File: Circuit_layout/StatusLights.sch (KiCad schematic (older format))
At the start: 33 parts, among them Q1 ZVP4525G, U1 PDM2-S24-S12, U11 TLP293, U12 TLP293, U16 LTC3638

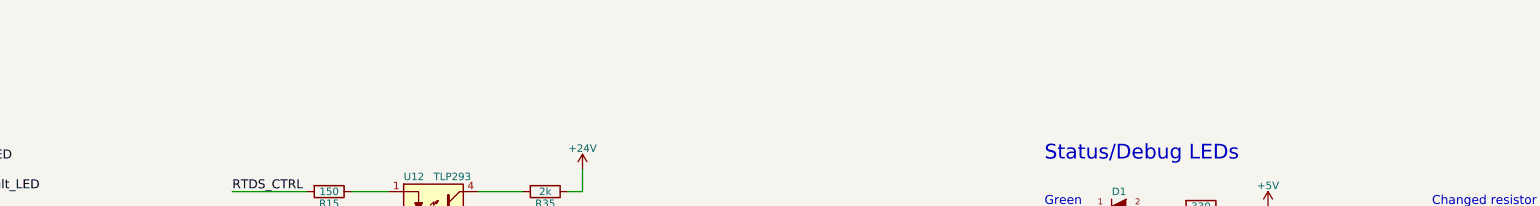
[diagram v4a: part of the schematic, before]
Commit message: reviewed schematic w/ prof. nadovich. proposed changes
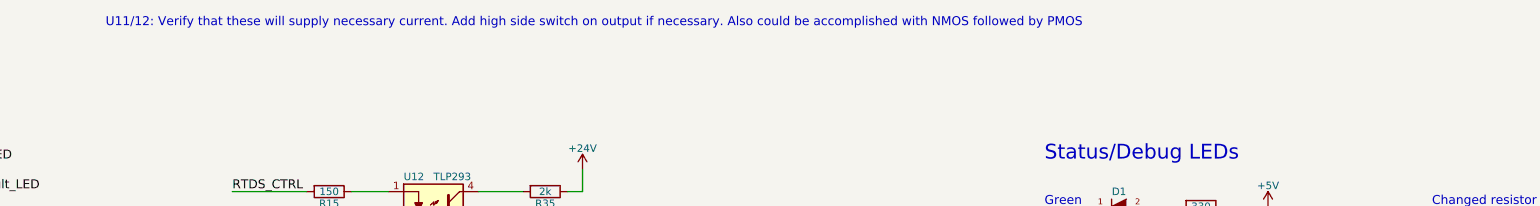
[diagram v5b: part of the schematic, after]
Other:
- note added: "U11/12: Verify that these will supply necessary current. Add high side switch on output if necessary. Also could be accomplished with NMOS followed by PMOS"
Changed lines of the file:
@@
 	6800 5200 6800 5300
 Connection ~ 6800 5300
+Text Notes 2450 -100 0    60   ~ 0
+U11/12: Verify that these will supply necessary current. Add high side switch on output if necessary. Also could be accomplished with NMOS followed by PMOS
 $EndSCHEMATC

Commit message: small changes
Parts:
- removed R84: 1k, Resistors_SMD:R_0805_HandSoldering, symbol R
- added R17: 10k, Resistors_SMD:R_0805_HandSoldering, symbol R
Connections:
- net IMD_Status: now also R17.2
- net at Q1.1 (G): now also R17.1
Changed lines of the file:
@@
 $EndComp
 $Comp
-L GND #PWR037
+L GND #PWR036
 U 1 1 58AF33D9
 P 4250 1300
-F 0 "#PWR037" H 4250 1050 50  0001 C CNN
+F 0 "#PWR036" H 4250 1050 50  0001 C CNN
 F 1 "GND" H 4250 1150 50  0000 C CNN
 F 2 "" H 4250 1300 50  0000 C CNN
@@
 $EndComp
 $Comp
-L +24V #PWR038
+L +24V #PWR037
 U 1 1 58AF3526
 P 5650 850
-F 0 "#PWR038" H 5650 700 50  0001 C CNN
+F 0 "#PWR037" H 5650 700 50  0001 C CNN
 F 1 "+24V" H 5650 990 50  0000 C CNN
 F 2 "" H 5650 850 50  0000 C CNN
@@
 $EndComp
 $Comp
-L GND #PWR039
+L GND #PWR038
 U 1 1 58AF4273
 P 4250 2500
-F 0 "#PWR039" H 4250 2250 50  0001 C CNN
+F 0 "#PWR038" H 4250 2250 50  0001 C CNN
 F 1 "GND" H 4250 2350 50  0000 C CNN
 F 2 "" H 4250 2500 50  0000 C CNN
@@
 $EndComp
 $Comp
-L +24V #PWR040
+L +24V #PWR039
 U 1 1 58AF427B
 P 5650 2000
-F 0 "#PWR040" H 5650 1850 50  0001 C CNN
+F 0 "#PWR039" H 5650 1850 50  0001 C CNN
 F 1 "+24V" H 5650 2140 50  0000 C CNN
 F 2 "" H 5650 2000 50  0000 C CNN
@@
 $EndComp
 $Comp
-L GND #PWR041
+L GND #PWR040
 U 1 1 58B26825
 P 8750 1200
-F 0 "#PWR041" H 8750 950 50  0001 C CNN
+F 0 "#PWR040" H 8750 950 50  0001 C CNN
 F 1 "GND" H 8750 1050 50  0000 C CNN
 F 2 "" H 8750 1200 50  0000 C CNN
@@
 $EndComp
 $Comp
-L GND #PWR042
+L GND #PWR041
 U 1 1 58B26F4E
 P 8750 1650
-F 0 "#PWR042" H 8750 1400 50  0001 C CNN
+F 0 "#PWR041" H 8750 1400 50  0001 C CNN
 F 1 "GND" H 8750 1500 50  0000 C CNN
 F 2 "" H 8750 1650 50  0000 C CNN
@@
 $EndComp
 $Comp
-L GND #PWR043
+L GND #PWR042
 U 1 1 58B272AA
 P 8750 2100
-F 0 "#PWR043" H 8750 1850 50  0001 C CNN
+F 0 "#PWR042" H 8750 1850 50  0001 C CNN
 F 1 "GND" H 8750 1950 50  0000 C CNN
 F 2 "" H 8750 2100 50  0000 C CNN
@@
 $EndComp
 $Comp
-L GND #PWR044
+L GND #PWR043
 U 1 1 58B27330
 P 8750 2550
-F 0 "#PWR044" H 8750 2300 50  0001 C CNN
+F 0 "#PWR043" H 8750 2300 50  0001 C CNN
 F 1 "GND" H 8750 2400 50  0000 C CNN
 F 2 "" H 8750 2550 50  0000 C CNN
@@
 Blue
 $Comp
-L +5V #PWR045
+L +5V #PWR044
 U 1 1 58B2809B
 P 10250 1100
-F 0 "#PWR045" H 10250 950 50  0001 C CNN
+F 0 "#PWR044" H 10250 950 50  0001 C CNN
 F 1 "+5V" H 10250 1240 50  0000 C CNN
 F 2 "" H 10250 1100 50  0000 C CNN
@@
 Text HLabel 1250 2200 0    60   Input ~ 0
 Spare_Blue
-$Comp
-L R R84
-U 1 1 58BBA9F7
-P 4200 3200
-F 0 "R84" V 4280 3200 50  0000 C CNN
-F 1 "1k" V 4200 3200 50  0000 C CNN
-F 2 "Resistors_SMD:R_0805_HandSoldering" V 4130 3200 50  0001 C CNN
-F 3 "" H 4200 3200 50  0000 C CNN
-F 4 "P1.00KCCT-ND" V 4200 3200 60  0001 C CNN "DigiKey P/N"
-F 5 "http://www.digikey.com/product-detail/en/panasonic-electronic-components/ERJ-6ENF1001V/P1.00KCCT-ND/118957" V 4200 3200 60  0001 C CNN "URL"
-F 6 "ERJ-6ENF1001V" V 4200 3200 60  0001 C CNN "Man P/N"
-	1    4200 3200
-	0    1    1    0
-$EndComp
 Text GLabel 1250 650  0    60   Input ~ 0
 RTDS
@@
 	4800 3550 4950 3550
 $Comp
-L +24V #PWR046
+L +24V #PWR045
 U 1 1 58C523A5
 P 4800 2750
-F 0 "#PWR046" H 4800 2600 50  0001 C CNN
+F 0 "#PWR045" H 4800 2600 50  0001 C CNN
 F 1 "+24V" H 4800 2890 50  0000 C CNN
 F 2 "" H 4800 2750 50  0000 C CNN
@@
 HV-
 $Comp
-L PWR_FLAG #FLG047
+L PWR_FLAG #FLG046
 U 1 1 58C1AF3D
 P 3600 5200
-F 0 "#FLG047" H 3600 5295 50  0001 C CNN
+F 0 "#FLG046" H 3600 5295 50  0001 C CNN
 F 1 "PWR_FLAG" H 3600 5380 50  0000 C CNN
 F 2 "" H 3600 5200 50  0000 C CNN
@@
 NoConn ~ 8650 5700
 $Comp
-L GND #PWR048
+L GND #PWR047
 U 1 1 58D3C796
 P 9400 5950
-F 0 "#PWR048" H 9400 5700 50  0001 C CNN
+F 0 "#PWR047" H 9400 5700 50  0001 C CNN
 F 1 "GND" H 9400 5800 50  0000 C CNN
 F 2 "" H 9400 5950 50  0000 C CNN
@@
 Text Notes 2450 -100 0    60   ~ 0
 U11/12: Verify that these will supply necessary current. Add high side switch on output if necessary. Also could be accomplished with NMOS followed by PMOS
+$Comp
+L R R17
+U 1 1 58D617C3
+P 4200 3200
+F 0 "R17" V 4280 3200 50  0000 C CNN
+F 1 "10k" V 4200 3200 50  0000 C CNN
+F 2 "Resistors_SMD:R_0805_HandSoldering" V 4130 3200 50  0001 C CNN
+F 3 "" H 4200 3200 50  0000 C CNN
+F 4 "P10.0KCCT-ND" V 4200 3200 60  0001 C CNN "DigiKey P/N"
+F 5 "http://www.digikey.com/product-detail/en/panasonic-electronic-components/ERJ-6ENF1002V/P10.0KCCT-ND/119248" V 4200 3200 60  0001 C CNN "URL"
+F 6 "ERJ-6ENF1002V" V 4200 3200 60  0001 C CNN "Man P/N"
+	1    4200 3200
+	0    1    1    0
+$EndComp
 $EndSCHEMATC

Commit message: organized sheet more, updated some footprints
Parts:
- U1: footprint Converters_DCDC_ACDC:DCDC-Conv_TRACO_TMR_1-xxxx_Single -> custom_footprints:DCDC-Conv_TRACO_TMR_1-xxxx_Single
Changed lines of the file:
@@
 $EndComp
 $Comp
-L GND #PWR033
+L GND #PWR031
 U 1 1 58AF33D9
 P 4250 1300
-F 0 "#PWR033" H 4250 1050 50  0001 C CNN
+F 0 "#PWR031" H 4250 1050 50  0001 C CNN
 F 1 "GND" H 4250 1150 50  0000 C CNN
 F 2 "" H 4250 1300 50  0000 C CNN
@@
 $EndComp
 $Comp
-L +24V #PWR034
+L +24V #PWR032
 U 1 1 58AF3526
 P 5650 850
-F 0 "#PWR034" H 5650 700 50  0001 C CNN
+F 0 "#PWR032" H 5650 700 50  0001 C CNN
 F 1 "+24V" H 5650 990 50  0000 C CNN
 F 2 "" H 5650 850 50  0000 C CNN
@@
 $EndComp
 $Comp
-L GND #PWR035
+L GND #PWR033
 U 1 1 58AF4273
 P 4250 2500
-F 0 "#PWR035" H 4250 2250 50  0001 C CNN
+F 0 "#PWR033" H 4250 2250 50  0001 C CNN
 F 1 "GND" H 4250 2350 50  0000 C CNN
 F 2 "" H 4250 2500 50  0000 C CNN
@@
 $EndComp
 $Comp
-L +24V #PWR036
+L +24V #PWR034
 U 1 1 58AF427B
 P 5650 2000
-F 0 "#PWR036" H 5650 1850 50  0001 C CNN
+F 0 "#PWR034" H 5650 1850 50  0001 C CNN
 F 1 "+24V" H 5650 2140 50  0000 C CNN
 F 2 "" H 5650 2000 50  0000 C CNN
@@
 $EndComp
 $Comp
-L GND #PWR037
+L GND #PWR035
 U 1 1 58B26825
 P 8750 1200
-F 0 "#PWR037" H 8750 950 50  0001 C CNN
+F 0 "#PWR035" H 8750 950 50  0001 C CNN
 F 1 "GND" H 8750 1050 50  0000 C CNN
 F 2 "" H 8750 1200 50  0000 C CNN
@@
 $EndComp
 $Comp
-L GND #PWR038
+L GND #PWR036
 U 1 1 58B26F4E
 P 8750 1650
-F 0 "#PWR038" H 8750 1400 50  0001 C CNN
+F 0 "#PWR036" H 8750 1400 50  0001 C CNN
 F 1 "GND" H 8750 1500 50  0000 C CNN
 F 2 "" H 8750 1650 50  0000 C CNN
@@
 $EndComp
 $Comp
-L GND #PWR039
+L GND #PWR037
 U 1 1 58B272AA
 P 8750 2100
-F 0 "#PWR039" H 8750 1850 50  0001 C CNN
+F 0 "#PWR037" H 8750 1850 50  0001 C CNN
 F 1 "GND" H 8750 1950 50  0000 C CNN
 F 2 "" H 8750 2100 50  0000 C CNN
@@
 $EndComp
 $Comp
-L GND #PWR040
+L GND #PWR038
 U 1 1 58B27330
 P 8750 2550
-F 0 "#PWR040" H 8750 2300 50  0001 C CNN
+F 0 "#PWR038" H 8750 2300 50  0001 C CNN
 F 1 "GND" H 8750 2400 50  0000 C CNN
 F 2 "" H 8750 2550 50  0000 C CNN
@@
 Blue
 $Comp
-L +5V #PWR041
+L +5V #PWR039
 U 1 1 58B2809B
 P 10250 1100
-F 0 "#PWR041" H 10250 950 50  0001 C CNN
+F 0 "#PWR039" H 10250 950 50  0001 C CNN
 F 1 "+5V" H 10250 1240 50  0000 C CNN
 F 2 "" H 10250 1100 50  0000 C CNN
@@
 	4800 3550 4950 3550
 $Comp
-L +24V #PWR042
+L +24V #PWR040
 U 1 1 58C523A5
 P 4800 2750
-F 0 "#PWR042" H 4800 2600 50  0001 C CNN
+F 0 "#PWR040" H 4800 2600 50  0001 C CNN
 F 1 "+24V" H 4800 2890 50  0000 C CNN
 F 2 "" H 4800 2750 50  0000 C CNN
@@
 HV-
 $Comp
-L PWR_FLAG #FLG043
+L PWR_FLAG #FLG041
 U 1 1 58C1AF3D
 P 3600 5200
-F 0 "#FLG043" H 3600 5295 50  0001 C CNN
+F 0 "#FLG041" H 3600 5295 50  0001 C CNN
 F 1 "PWR_FLAG" H 3600 5380 50  0000 C CNN
 F 2 "" H 3600 5200 50  0000 C CNN
@@
 F 0 "U1" H 7900 5600 50  0000 C CNN
 F 1 "PDM2-S24-S12" H 7900 5900 50  0000 C CNN
-F 2 "Converters_DCDC_ACDC:DCDC-Conv_TRACO_TMR_1-xxxx_Single" H 7900 5300 50  0001 C CNN
+F 2 "custom_footprints:DCDC-Conv_TRACO_TMR_1-xxxx_Single" H 7900 5300 50  0001 C CNN
 F 3 "" H 7900 5200 50  0001 C CNN
 F 4 "102-2728-ND" H 7900 5700 60  0001 C CNN "DigiKey P/N"
@@
 NoConn ~ 8650 5700
 $Comp
-L GND #PWR044
+L GND #PWR042
 U 1 1 58D3C796
 P 9400 5950
-F 0 "#PWR044" H 9400 5700 50  0001 C CNN
+F 0 "#PWR042" H 9400 5700 50  0001 C CNN
 F 1 "GND" H 9400 5800 50  0000 C CNN
 F 2 "" H 9400 5950 50  0000 C CNN
